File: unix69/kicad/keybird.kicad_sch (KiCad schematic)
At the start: 139 parts, among them SW00 SW_Push, SW01 SW_Push, SW02 SW_Push, SW03 SW_Push, SW04 SW_Push, SW05 SW_Push, SW06 SW_Push, SW07 SW_Push, SW10 SW_Push, SW11 SW_Push, SW12 SW_Push, SW13 SW_Push, SW14 SW_Push, SW15 SW_Push, SW16 SW_Push, SW17 SW_Push, SW20 SW_Push, SW21 SW_Push, SW22 SW_Push, SW23 SW_Push, SW24 SW_Push, SW25 SW_Push, SW26 SW_Push, SW27 SW_Push, SW30 SW_Push, SW31 SW_Push, SW32 SW_Push, SW33 SW_Push, SW34 SW_Push, SW35 SW_Push, SW36 SW_Push, SW40 SW_Push, SW41 SW_Push, SW42 SW_Push, SW43 SW_Push, SW44 SW_Push, SW45 SW_Push, SW47 SW_Push, SW50 SW_Push, SW51 SW_Push, SW52 SW_Push, SW53 SW_Push, SW54 SW_Push, SW55 SW_Push, SW56 SW_Push, SW57 SW_Push, SW60 SW_Push, SW61 SW_Push, SW62 SW_Push, SW63 SW_Push, SW64 SW_Push, SW65 SW_Push, SW66 SW_Push, SW67 SW_Push, SW70 SW_Push, SW71 SW_Push, SW72 SW_Push, SW73 SW_Push, SW74 SW_Push, SW75 SW_Push, SW76 SW_Push, SW77 SW_Push, SW80 SW_Push, SW81 SW_Push, SW83 SW_Push, SW84 SW_Push, SW85 SW_Push, SW86 SW_Push, SW87 SW_Push, U0 RP2040-Tiny

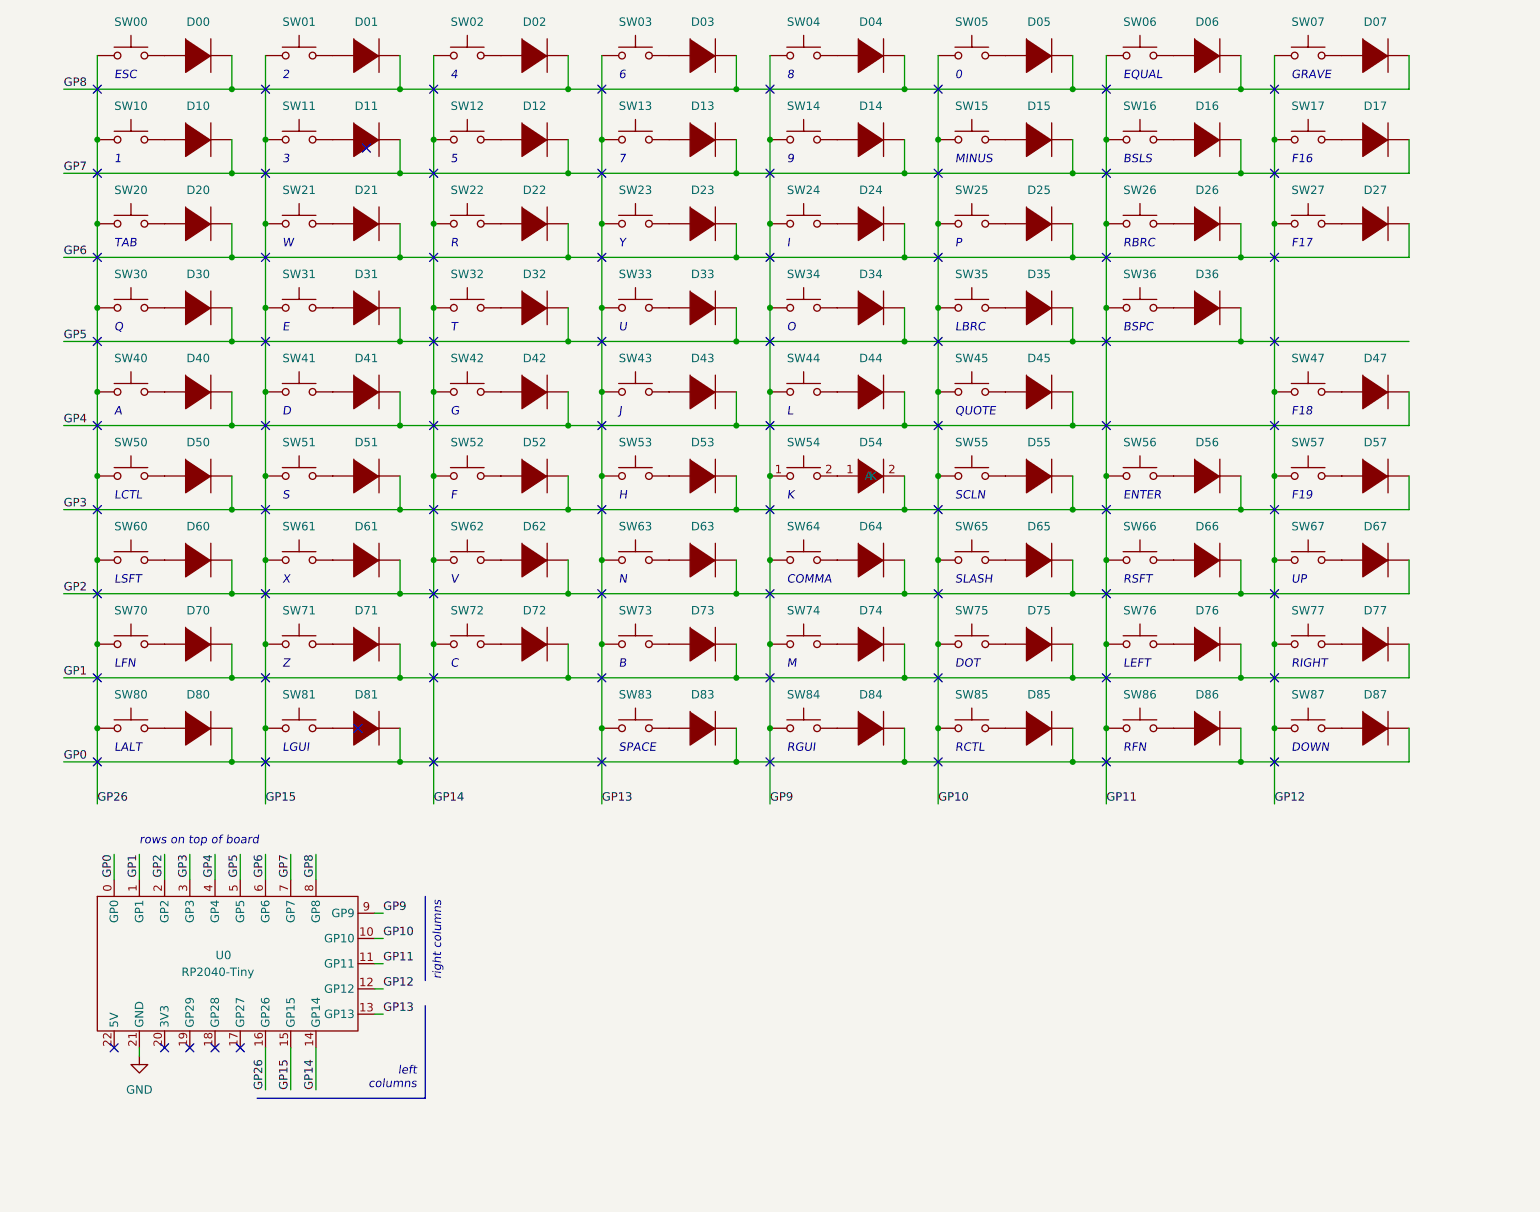
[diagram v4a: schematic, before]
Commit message: much pcb fettling
silkscreen key names from schematic

diode placement wrt switch connections
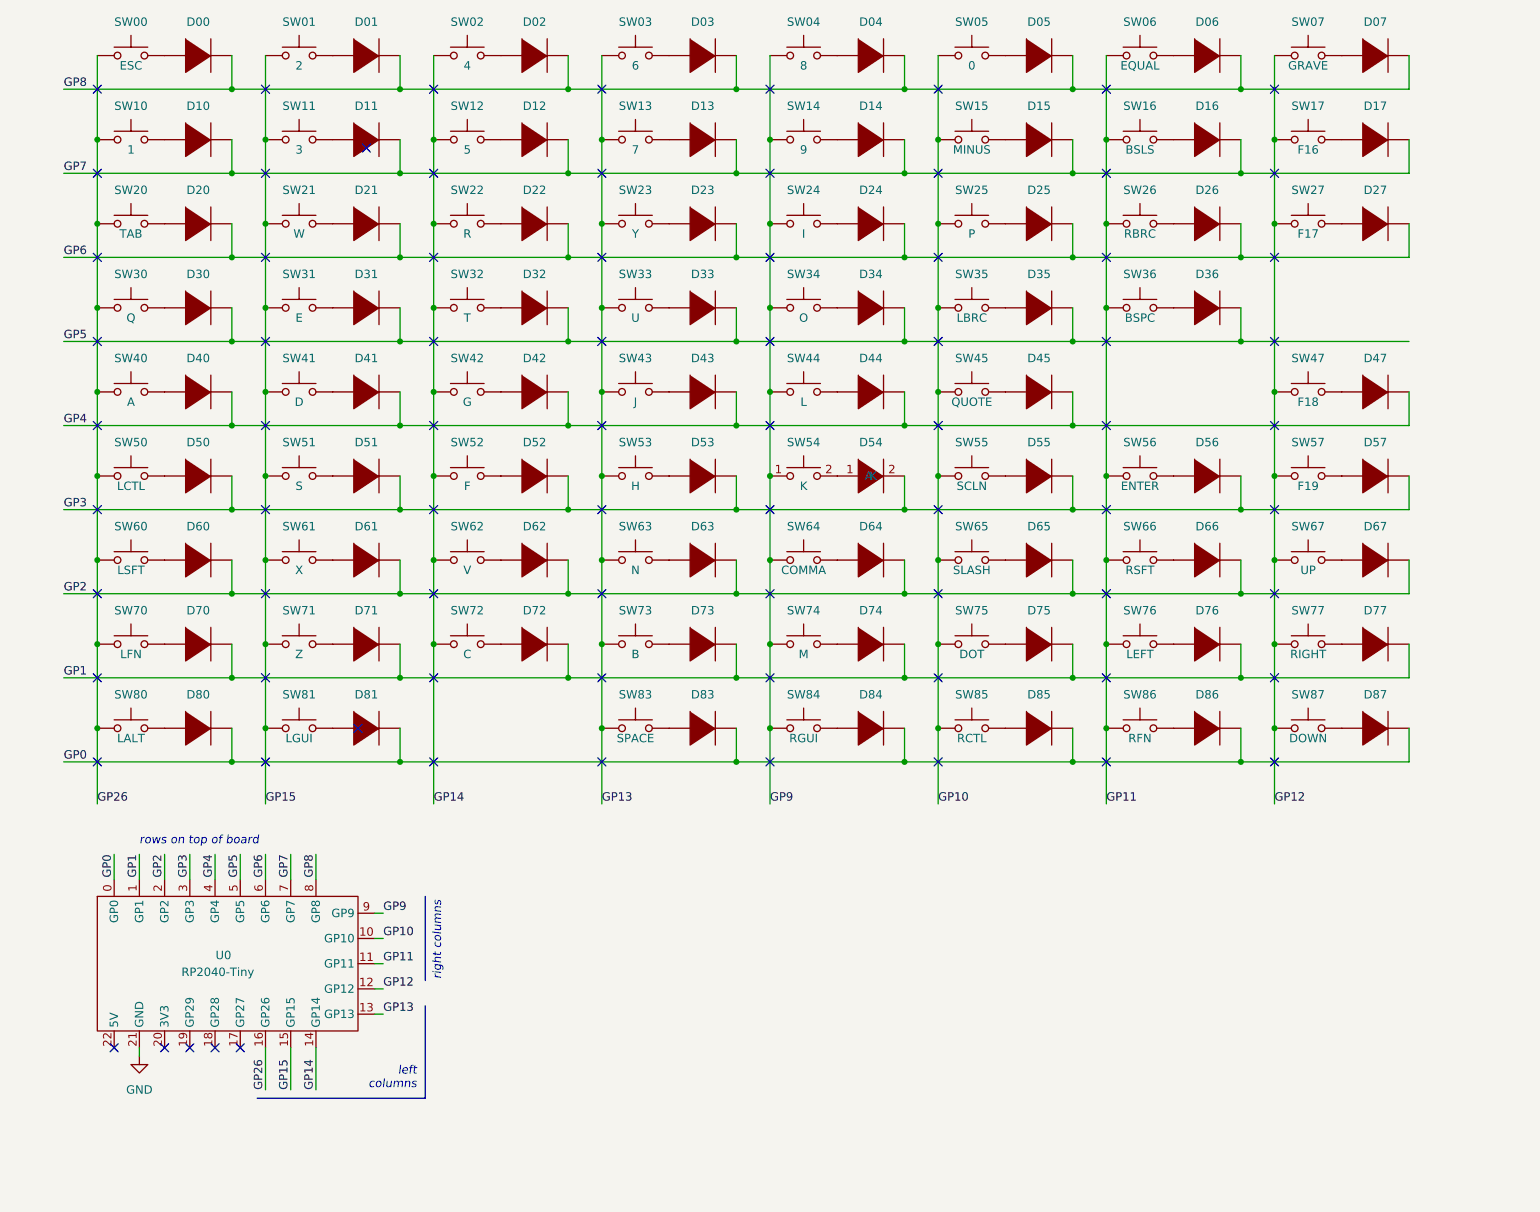
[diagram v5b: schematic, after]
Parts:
- SW00: value SW_Push -> ESC
- SW01: value SW_Push -> 2
- SW02: value SW_Push -> 4
- SW03: value SW_Push -> 6
- SW04: value SW_Push -> 8
- SW05: value SW_Push -> 0
- SW06: value SW_Push -> EQUAL
- SW07: value SW_Push -> GRAVE
- SW10: value SW_Push -> 1
- SW11: value SW_Push -> 3
- SW12: value SW_Push -> 5
- SW13: value SW_Push -> 7
- SW14: value SW_Push -> 9
- SW15: value SW_Push -> MINUS
- SW16: value SW_Push -> BSLS
- SW17: value SW_Push -> F16
- SW20: value SW_Push -> TAB
- SW21: value SW_Push -> W
- SW22: value SW_Push -> R
- SW23: value SW_Push -> Y
- SW24: value SW_Push -> I
- SW25: value SW_Push -> P
- SW26: value SW_Push -> RBRC
- SW27: value SW_Push -> F17
- SW30: value SW_Push -> Q
- SW31: value SW_Push -> E
- SW32: value SW_Push -> T
- SW33: value SW_Push -> U
- SW34: value SW_Push -> O
- SW35: value SW_Push -> LBRC
- SW36: value SW_Push -> BSPC
- SW40: value SW_Push -> A
- SW41: value SW_Push -> D
- SW42: value SW_Push -> G
- SW43: value SW_Push -> J
- SW44: value SW_Push -> L
- SW45: value SW_Push -> QUOTE
- SW47: value SW_Push -> F18
- SW50: value SW_Push -> LCTL
- SW51: value SW_Push -> S
- SW52: value SW_Push -> F
- SW53: value SW_Push -> H
- SW54: value SW_Push -> K
- SW55: value SW_Push -> SCLN
- SW56: value SW_Push -> ENTER
- SW57: value SW_Push -> F19
- SW60: value SW_Push -> LSFT
- SW61: value SW_Push -> X
- SW62: value SW_Push -> V
- SW63: value SW_Push -> N
- SW64: value SW_Push -> COMMA
- SW65: value SW_Push -> SLASH
- SW66: value SW_Push -> RSFT
- SW67: value SW_Push -> UP
- SW70: value SW_Push -> LFN
- SW71: value SW_Push -> Z
- SW72: value SW_Push -> C
- SW73: value SW_Push -> B
- SW74: value SW_Push -> M
- SW75: value SW_Push -> DOT
- SW76: value SW_Push -> LEFT
- SW77: value SW_Push -> RIGHT
- SW80: value SW_Push -> LALT
- SW81: value SW_Push -> LGUI
- SW83: value SW_Push -> SPACE
- SW84: value SW_Push -> RGUI
- SW85: value SW_Push -> RCTL
- SW86: value SW_Push -> RFN
- SW87: value SW_Push -> DOWN
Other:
- note removed: "0"
- note removed: "1"
- note removed: "2"
- note removed: "3"
- note removed: "4"
- note removed: "5"
- note removed: "6"
- note removed: "7"
- note removed: "8"
- note removed: "9"
- note removed: "A"
- note removed: "B"
- note removed: "BSLS"
- note removed: "BSPC"
- note removed: "C"
- note removed: "COMMA"
- note removed: "D"
- note removed: "DOT"
- note removed: "DOWN"
- note removed: "E"
- note removed: "ENTER"
- note removed: "EQUAL"
- note removed: "ESC"
- note removed: "F"
- note removed: "F16"
- note removed: "F17"
- note removed: "F18"
- note removed: "F19"
- note removed: "G"
- note removed: "GRAVE"
- note removed: "H"
- note removed: "I"
- note removed: "J"
- note removed: "K"
- note removed: "L"
- note removed: "LALT"
- note removed: "LBRC"
- note removed: "LCTL"
- note removed: "LEFT"
- note removed: "LFN"
- note removed: "LGUI"
- note removed: "LSFT"
- note removed: "M"
- note removed: "MINUS"
- note removed: "N"
- note removed: "O"
- note removed: "P"
- note removed: "Q"
- note removed: "QUOTE"
- note removed: "R"
- note removed: "RBRC"
- note removed: "RCTL"
- note removed: "RFN"
- note removed: "RGUI"
- note removed: "RIGHT"
- note removed: "RSFT"
- note removed: "S"
- note removed: "SCLN"
- note removed: "SLASH"
- note removed: "SPACE"
- note removed: "T"
- note removed: "TAB"
- note removed: "U"
- note removed: "UP"
- note removed: "V"
- note removed: "W"
- note removed: "X"
- note removed: "Y"
- note removed: "Z"

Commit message: redo the row lines on the front of the board
much nicer!
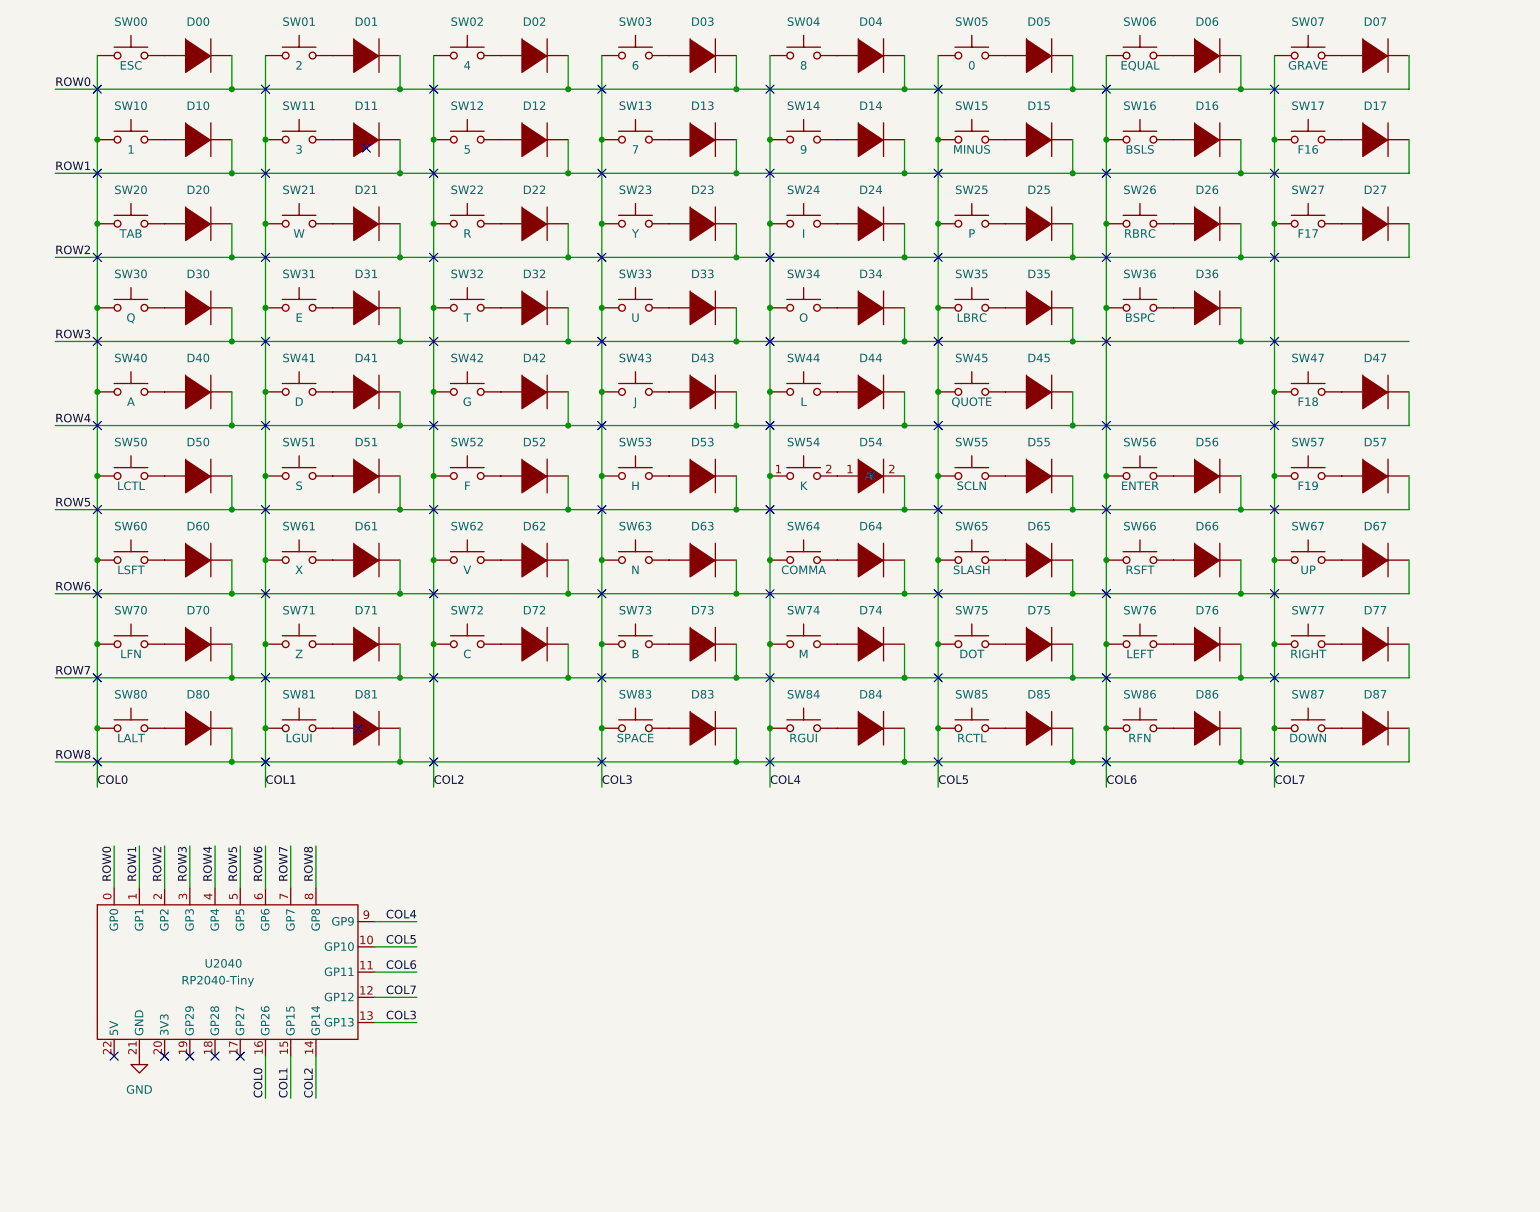
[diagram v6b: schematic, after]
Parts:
- renumbered U0 to U2040
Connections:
- net GP0 renamed ROW8
- net ROW8: now also U2040.8 (GP8); no longer U2040.0 (GP0)
- net GP1 renamed ROW7
- net ROW7: now also U2040.7 (GP7); no longer U2040.1 (GP1)
- net GP10 renamed COL5
- net GP11 renamed COL6
- net GP12 renamed COL7
- net GP13 renamed COL3
- net GP14 renamed COL2
- net GP15 renamed COL1
- net GP2 renamed ROW6
- net ROW6: now also U2040.6 (GP6); no longer U2040.2 (GP2)
- net GP26 renamed COL0
- net GP3 renamed ROW5
- net ROW5: now also U2040.5 (GP5); no longer U2040.3 (GP3)
- net GP4 renamed ROW4
- net GP5 renamed ROW3
- net ROW3: now also U2040.3 (GP3); no longer U2040.5 (GP5)
- net GP6 renamed ROW2
- net ROW2: now also U2040.2 (GP2); no longer U2040.6 (GP6)
- net GP7 renamed ROW1
- net ROW1: now also U2040.1 (GP1); no longer U2040.7 (GP7)
- net GP8 renamed ROW0
- net ROW0: now also U2040.0 (GP0); no longer U2040.8 (GP8)
- net GP9 renamed COL4
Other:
- note removed: "left columns"
- note removed: "right columns"
- note removed: "rows on top of board"
- moved on the sheet: U2040

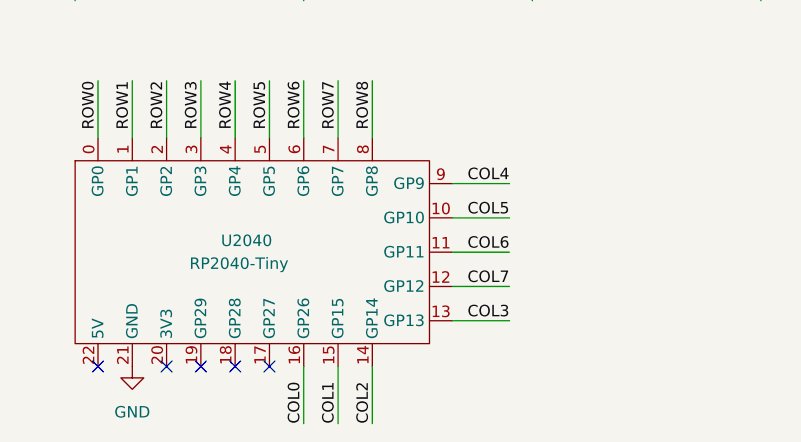
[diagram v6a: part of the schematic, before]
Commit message: done? no drc errors!
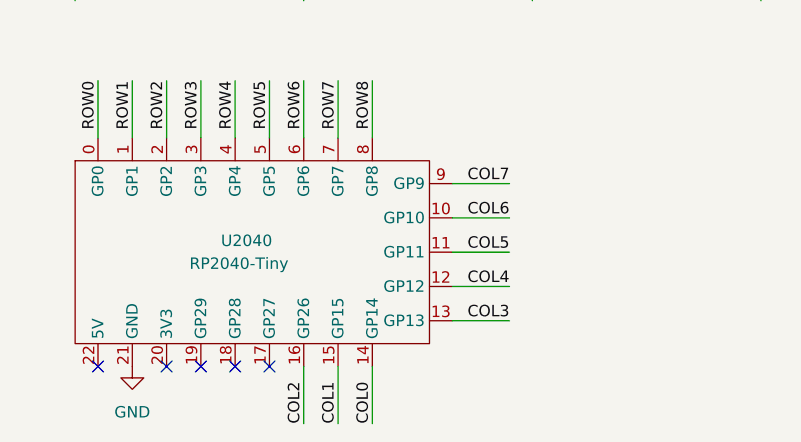
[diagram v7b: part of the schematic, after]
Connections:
- net COL0: now also U2040.14 (GP14); no longer U2040.16 (GP26)
- net COL2: now also U2040.16 (GP26); no longer U2040.14 (GP14)
- net COL4: now also U2040.12 (GP12); no longer U2040.9 (GP9)
- net COL5: now also U2040.11 (GP11); no longer U2040.10 (GP10)
- net COL6: now also U2040.10 (GP10); no longer U2040.11 (GP11)
- net COL7: now also U2040.9 (GP9); no longer U2040.12 (GP12)
